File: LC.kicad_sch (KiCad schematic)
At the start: 89 parts, among them J1 INPUT+, J10 DISPLAY, J11 ENTER_BUTTON, J12 UP_BUTTON, J2 INPUT-, J3 Barrel_Jack, J4 EXT_CLK, J5 CLKSRC, J6 SIGSRC, J7 EXT_SIG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

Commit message: forgot that polystyrene are THT
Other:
- note added: "C0G (NP0)"
- note removed: "Polystyrene"
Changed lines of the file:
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@@
     (effects (font (size 1.27 1.27)) (justify left bottom))
   )
-  (text "Polystyrene" (at 97.79 92.075 0)
+  (text "C0G (NP0)" (at 97.79 92.075 0)
     (effects (font (size 1.27 1.27)) (justify left bottom))
   )
@@
     (effects (font (size 1.27 1.27)) (justify left bottom))
   )
-  (text "Polystyrene" (at 102.87 77.47 0)
+  (text "C0G (NP0)" (at 102.87 77.47 0)
     (effects (font (size 1.27 1.27)) (justify left bottom))
   )

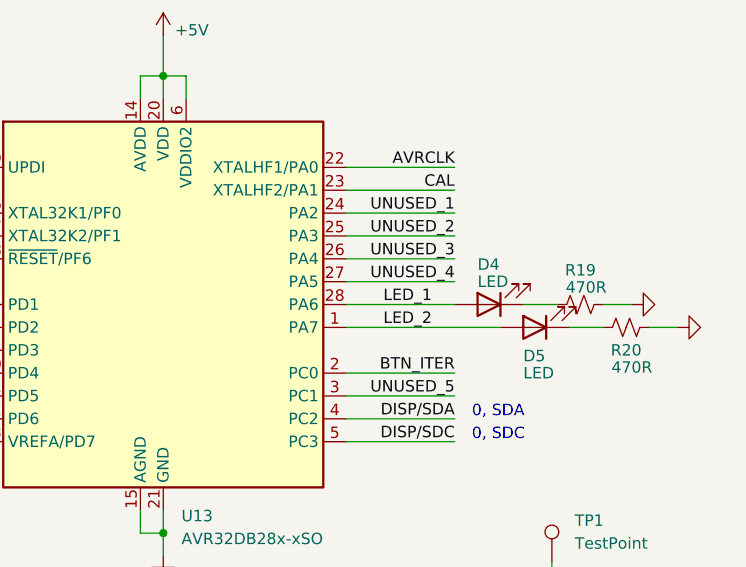
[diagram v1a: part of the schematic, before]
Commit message: a few more pin swaps
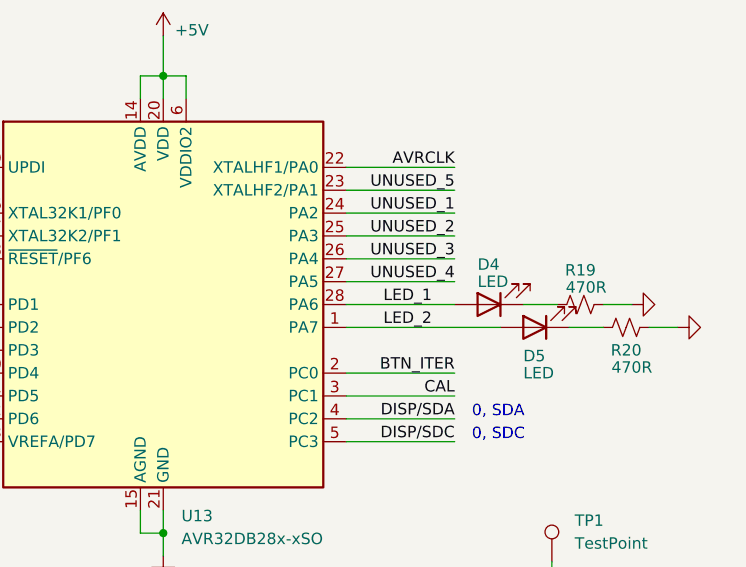
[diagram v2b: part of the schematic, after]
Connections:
- net CAL: now also U13.3 (PC1); no longer U13.23 (XTALHF2/PA1)
- net UNUSED_5: now also U13.23 (XTALHF2/PA1); no longer U13.3 (PC1)
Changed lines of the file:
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@@
     (effects (font (size 1.27 1.27)) (justify left bottom))
   )
-  (label "CAL" (at 367.665 73.025 180)
+  (label "CAL" (at 367.665 95.885 180)
     (effects (font (size 1.27 1.27)) (justify right bottom))
   )
@@
     (effects (font (size 1.27 1.27)) (justify left bottom))
   )
-  (label "UNUSED_5" (at 367.665 95.885 180)
+  (label "UNUSED_5" (at 367.665 73.025 180)
     (effects (font (size 1.27 1.27)) (justify right bottom))
   )
